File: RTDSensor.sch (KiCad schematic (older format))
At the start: 6 parts

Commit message: Addressed review.
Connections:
- net GNDPWR renamed GNDREF

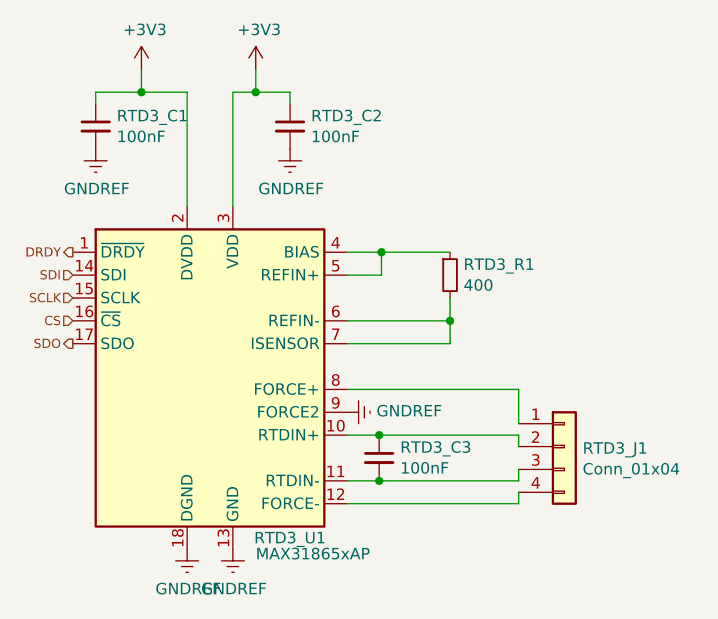
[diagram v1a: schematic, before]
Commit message: Updated README with assembly and testing instructions.
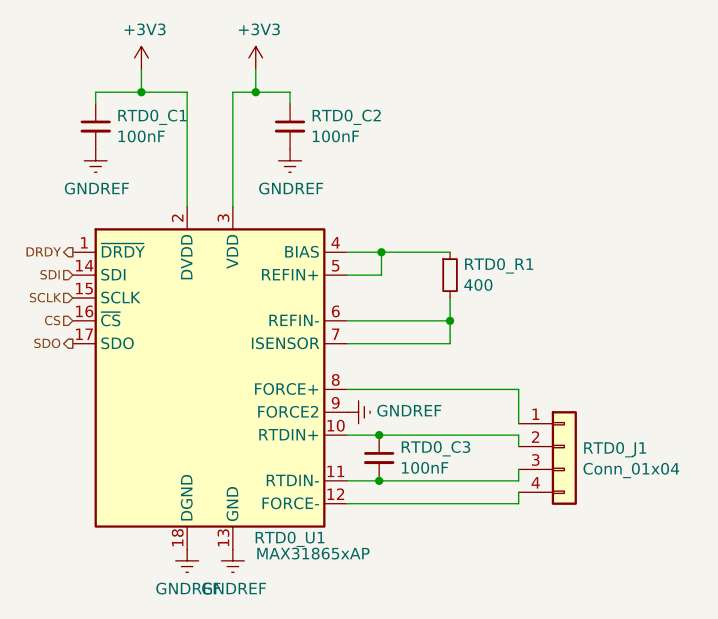
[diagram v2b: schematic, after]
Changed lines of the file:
@@
 EELAYER 30 0
 EELAYER END
-$Descr A4 11693 8268
+$Descr USLetter 11000 8500
 encoding utf-8
-Sheet 5 9
-Title "RTD Sensor subsheet."
-Date "2020-12-08"
-Rev "Rev 1.0"
-Comp "UT Solar Vehicles Team"
+Sheet 3 9
+Title "Array RTD/Irradiance Sensor Board"
+Date "2020-12-13"
+Rev "1.0.0"
+Comp "UT Solar Vehicle Team"
 Comment1 "Matthew Yu"
-Comment2 "Jacob Giddens"
-Comment3 "Prof. Gary Hallock"
+Comment2 "Gary Hallock"
+Comment3 "Jacob Giddens"
 Comment4 ""
 $EndDescr
@@
 AR Path="/60443CC8/60039171" Ref="#PWR073"  Part="1"
 AR Path="/60443CD9/60039171" Ref="#PWR080"  Part="1"
-F 0 "#PWR080" H 3840 1490 50  0001 C CNN
+F 0 "#PWR031" H 3840 1490 50  0001 C CNN
 F 1 "+3V3" H 3855 1813 50  0000 C CNN
 F 2 "" H 3840 1640 50  0001 C CNN
@@
 AR Path="/60443CC8/6003917E" Ref="#PWR070"  Part="1"
 AR Path="/60443CD9/6003917E" Ref="#PWR077"  Part="1"
-F 0 "#PWR077" H 3340 1490 50  0001 C CNN
+F 0 "#PWR019" H 3340 1490 50  0001 C CNN
 F 1 "+3V3" H 3355 1813 50  0000 C CNN
 F 2 "" H 3340 1640 50  0001 C CNN
@@
 AR Path="/60443CC8/60039195" Ref="RTD6_U1"  Part="1"
 AR Path="/60443CD9/60039195" Ref="RTD7_U1"  Part="1"
-F 0 "RTD3_U1" H 3990 2390 50  0000 C CNN
+F 0 "RTD0_U1" H 3990 2390 50  0000 C CNN
 F 1 "MAX31865xAP" H 4090 2320 50  0000 C CNN
 F 2 "Package_SO:SSOP-20_5.3x7.2mm_P0.65mm" H 3790 2390 50  0001 L CNN
@@
 AR Path="/60443CC8/600391AD" Ref="RTD6_J1"  Part="1"
 AR Path="/60443CD9/600391AD" Ref="RTD7_J1"  Part="1"
-F 0 "RTD3_J1" H 5270 3282 50  0000 L CNN
+F 0 "RTD0_J1" H 5270 3282 50  0000 L CNN
 F 1 "Conn_01x04" H 5270 3191 50  0000 L CNN
 F 2 "Connector_Molex:Molex_Micro-Fit_3.0_43650-0415_1x04_P3.00mm_Vertical" H 5190 3290 50  0001 C CNN
@@
 AR Path="/60443CC8/600391C5" Ref="RTD6_R1"  Part="1"
 AR Path="/60443CD9/600391C5" Ref="RTD7_R1"  Part="1"
-F 0 "RTD3_R1" H 4749 2586 50  0000 L CNN
+F 0 "RTD0_R1" H 4749 2586 50  0000 L CNN
 F 1 "400" H 4749 2495 50  0000 L CNN
 F 2 "Resistor_SMD:R_0805_2012Metric" H 4690 2540 50  0001 C CNN
@@
 AR Path="/60443CC8/600391B5" Ref="RTD6_C3"  Part="1"
 AR Path="/60443CD9/600391B5" Ref="RTD7_C3"  Part="1"
-F 0 "RTD3_C3" H 4472 3386 50  0000 L CNN
+F 0 "RTD0_C3" H 4472 3386 50  0000 L CNN
 F 1 "100nF" H 4472 3295 50  0000 L CNN
 F 2 "Capacitor_SMD:C_0805_2012Metric" H 4380 3340 50  0001 C CNN
@@
 AR Path="/60443CC8/60039165" Ref="RTD6_C2"  Part="1"
 AR Path="/60443CD9/60039165" Ref="RTD7_C2"  Part="1"
-F 0 "RTD3_C2" H 4082 1936 50  0000 L CNN
+F 0 "RTD0_C2" H 4082 1936 50  0000 L CNN
 F 1 "100nF" H 4082 1845 50  0000 L CNN
 F 2 "Capacitor_SMD:C_0805_2012Metric" H 3990 1890 50  0001 C CNN
@@
 AR Path="/60443CC8/6003918F" Ref="RTD6_C1"  Part="1"
 AR Path="/60443CD9/6003918F" Ref="RTD7_C1"  Part="1"
-F 0 "RTD3_C1" H 3232 1936 50  0000 L CNN
+F 0 "RTD0_C1" H 3232 1936 50  0000 L CNN
 F 1 "100nF" H 3232 1845 50  0000 L CNN
 F 2 "Capacitor_SMD:C_0805_2012Metric" H 3140 1890 50  0001 C CNN
@@
 AR Path="/60443CB7/5FEE301D" Ref="#PWR0125"  Part="1"
 AR Path="/60443CD9/5FEE301D" Ref="#PWR0137"  Part="1"
-F 0 "#PWR0137" H 3540 3490 50  0001 C CNN
+F 0 "#PWR0113" H 3540 3490 50  0001 C CNN
 F 1 "GNDREF" H 3545 3567 50  0000 C CNN
 F 2 "" H 3540 3740 50  0001 C CNN
@@
 AR Path="/60443CB7/5FEE6AF3" Ref="#PWR0126"  Part="1"
 AR Path="/60443CD9/5FEE6AF3" Ref="#PWR0138"  Part="1"
-F 0 "#PWR0138" H 3740 3490 50  0001 C CNN
+F 0 "#PWR0114" H 3740 3490 50  0001 C CNN
 F 1 "GNDREF" H 3745 3567 50  0000 C CNN
 F 2 "" H 3740 3740 50  0001 C CNN
@@
 AR Path="/60443CB7/5FEE8B63" Ref="#PWR0127"  Part="1"
 AR Path="/60443CD9/5FEE8B63" Ref="#PWR0139"  Part="1"
-F 0 "#PWR0139" H 3140 1740 50  0001 C CNN
+F 0 "#PWR0115" H 3140 1740 50  0001 C CNN
 F 1 "GNDREF" H 3145 1817 50  0000 C CNN
 F 2 "" H 3140 1990 50  0001 C CNN
@@
 AR Path="/60443CB7/5FEED197" Ref="#PWR0128"  Part="1"
 AR Path="/60443CD9/5FEED197" Ref="#PWR0140"  Part="1"
-F 0 "#PWR0140" H 3990 1740 50  0001 C CNN
+F 0 "#PWR0116" H 3990 1740 50  0001 C CNN
 F 1 "GNDREF" H 3995 1817 50  0000 C CNN
 F 2 "" H 3990 1990 50  0001 C CNN
@@
 AR Path="/60443CB7/5FEF5EC0" Ref="#PWR0145"  Part="1"
 AR Path="/60443CD9/5FEF5EC0" Ref="#PWR0148"  Part="1"
-F 0 "#PWR0148" H 4240 2890 50  0001 C CNN
+F 0 "#PWR0142" H 4240 2890 50  0001 C CNN
 F 1 "GNDREF" V 4245 3012 50  0000 R CNN
 F 2 "" H 4240 3140 50  0001 C CNN
